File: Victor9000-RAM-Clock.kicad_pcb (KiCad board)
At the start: 2 copper layers, 1 part

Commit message: Layout
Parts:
- removed REF**: Victor 9000 Expansion Edge Connector, victor-exp:Victor Expansion Edge Connector
- added C1: 100n, Capacitor_THT:C_Disc_D5.0mm_W2.5mm_P2.50mm, F.Cu at (141.0, 83.8)
- added C2: 100n, Capacitor_THT:C_Disc_D5.0mm_W2.5mm_P2.50mm, F.Cu at (134.7, 132.1)
- added C3: 100n, Capacitor_THT:C_Disc_D5.0mm_W2.5mm_P2.50mm, F.Cu at (148.6, 132.1)
- added C4: 100n, Capacitor_THT:C_Disc_D5.0mm_W2.5mm_P2.50mm, F.Cu at (162.6, 132.1)
- added C5: 100n, Capacitor_THT:C_Disc_D5.0mm_W2.5mm_P2.50mm, F.Cu at (88.9, 132.1)
- added C6: 100n, Capacitor_THT:C_Disc_D5.0mm_W2.5mm_P2.50mm, F.Cu at (113.1, 132.1)
- added C7: 100n, Capacitor_THT:C_Disc_D5.0mm_W2.5mm_P2.50mm, F.Cu at (141.0, 96.5)
- added C8: 10u, Capacitor_THT:CP_Radial_D4.0mm_P1.50mm, F.Cu at (142.2, 132.1)
- added H1: Expansion_Connector, victor-exp:Victor Expansion Edge Connector, F.Cu at (108.0, 138.4)
- added JP1: Jumper, Connector_PinHeader_2.54mm:PinHeader_1x02_P2.54mm_Vertical, F.Cu at (127.0, 115.6)
- added R1: 10k, Resistor_THT:R_Axial_DIN0207_L6.3mm_D2.5mm_P7.62mm_Horizontal, F.Cu at (127.0, 132.1)
- added U1: 74LS00, Package_DIP:DIP-14_W7.62mm, F.Cu at (167.6, 127.0)
- added U2: 74LS11, Package_DIP:DIP-14_W7.62mm, F.Cu at (153.7, 127.0)
- added U3: 74LS139, Package_DIP:DIP-16_W7.62mm, F.Cu at (139.7, 127.0)
- added U4: 74LS373, Package_DIP:DIP-20_W7.62mm, F.Cu at (144.8, 104.1)
- added U5: AS6C4008-55PCN, Package_DIP:DIP-32_W15.24mm, F.Cu at (121.9, 127.0)
- added U6: 74LS245, Package_DIP:DIP-20_W7.62mm, F.Cu at (144.8, 91.4)
- added U7: AS6C4008-55PCN, Package_DIP:DIP-32_W15.24mm, F.Cu at (97.8, 127.0)
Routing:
- net /DT_~R: track 0.00 -> 115.4 mm, vias 0 -> 2
- net /ALE: track 0.00 -> 100.9 mm, vias 0 -> 2
- net /DQ7: track 0.00 -> 98.4 mm
- net /DQ6: track 0.00 -> 90.8 mm
- net /~EN2: track 0.00 -> 88.2 mm, vias 0 -> 1
- net /A19: track 0.00 -> 86.7 mm, vias 0 -> 1
- net /A17: track 0.00 -> 83.7 mm, vias 0 -> 1
- net /DQ5: track 0.00 -> 83.2 mm
- net /DQ0: track 0.00 -> 78.8 mm
- net /A7: track 0.00 -> 78.8 mm, vias 0 -> 1
- net /~EN1: track 0.00 -> 77.7 mm, vias 0 -> 1
- net /A3: track 0.00 -> 76.3 mm
- net /DQ4: track 0.00 -> 75.5 mm
- net /A18: track 0.00 -> 71.5 mm
- net /DQ1: track 0.00 -> 71.2 mm
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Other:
- net class Default: clearance 0.2 -> 0.254; trace_width 0.25 -> 0.254; via_dia 0.8 -> 0.762; via_drill 0.4 -> 0.381
- rule trace_clearance: 0.2 -> 0.254

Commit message: Routing completed
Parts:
- moved C3 26.5 mm to (159.4, 107.9), turned to 90 degrees
- moved C4 25.2 mm to (179.1, 113.0)
- moved C6 25.2 mm to (129.6, 113.0)
- moved C5 25.2 mm to (105.5, 113.0)
- moved U1 25.2 mm to (184.2, 108.0)
- moved U2 25.2 mm to (170.2, 108.0)
- moved U3 25.2 mm to (156.2, 108.0)
- moved C2 25.2 mm to (151.2, 113.0)
- moved H1 25.2 mm to (124.5, 119.4)
- moved R1 25.2 mm to (143.5, 113.0)
- moved U5 25.2 mm to (138.4, 108.0)
- moved C1 25.2 mm to (157.5, 64.8)
- moved C7 25.2 mm to (157.5, 77.5)
- moved JP1 25.2 mm to (143.5, 96.5)
- moved U4 25.2 mm to (161.3, 85.1)
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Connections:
- H1 pad 31: Net-(H1-Pad31) -> GND
- H1 pad 35: Net-(H1-Pad35) -> GND
- H1 pad 36: Net-(H1-Pad36) -> +5V
- H1 pad 39: Net-(H1-Pad39) -> GND
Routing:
- net +5V: track 0.00 -> 76.3 mm, vias 0 -> 2
- net GND: track 0.00 -> 41.2 mm, vias 0 -> 1
- added copper zone on F.Cu, net +5V
- added copper zone on B.Cu, net GND
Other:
- board outline added: 94 x 68.6 mm
- board text added: "Victor 9000 RAM Expansion v01 (c) Florian Reitz 2021"
- board text added: "v01"

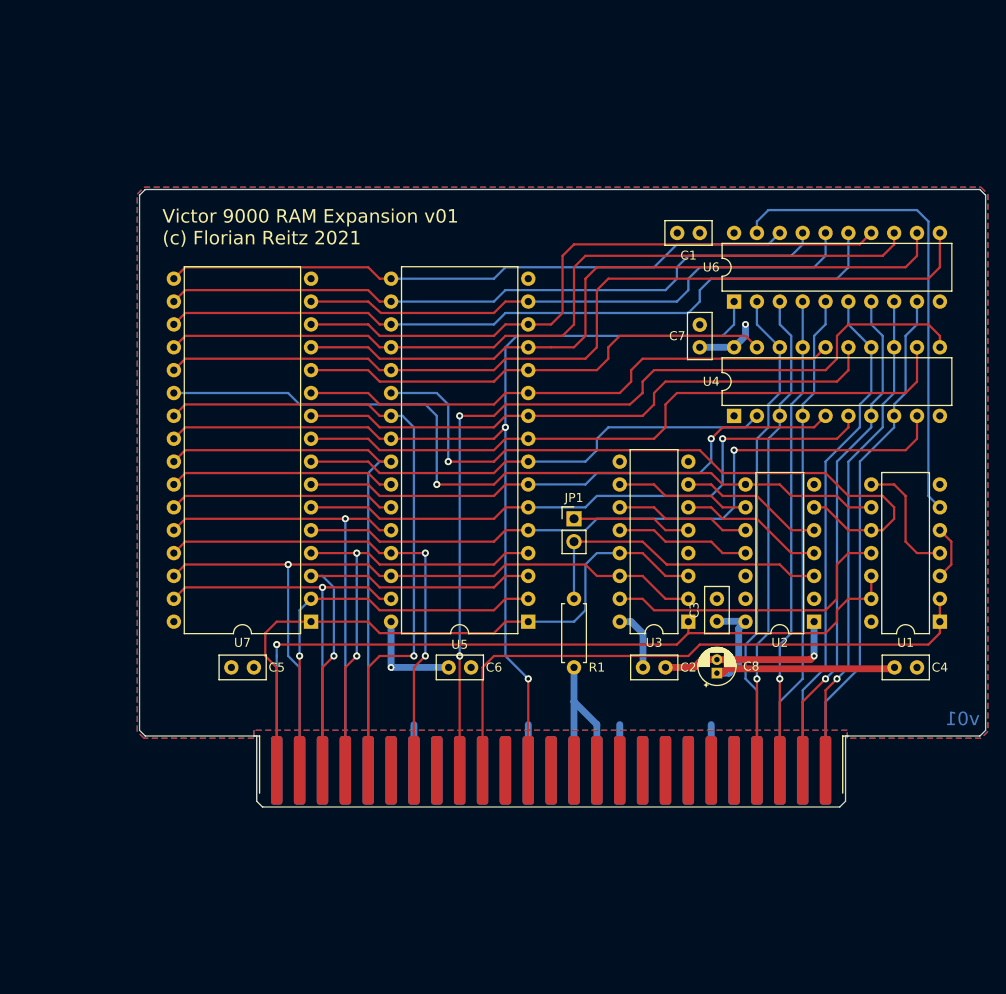
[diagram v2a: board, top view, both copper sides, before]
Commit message: DS1315 added
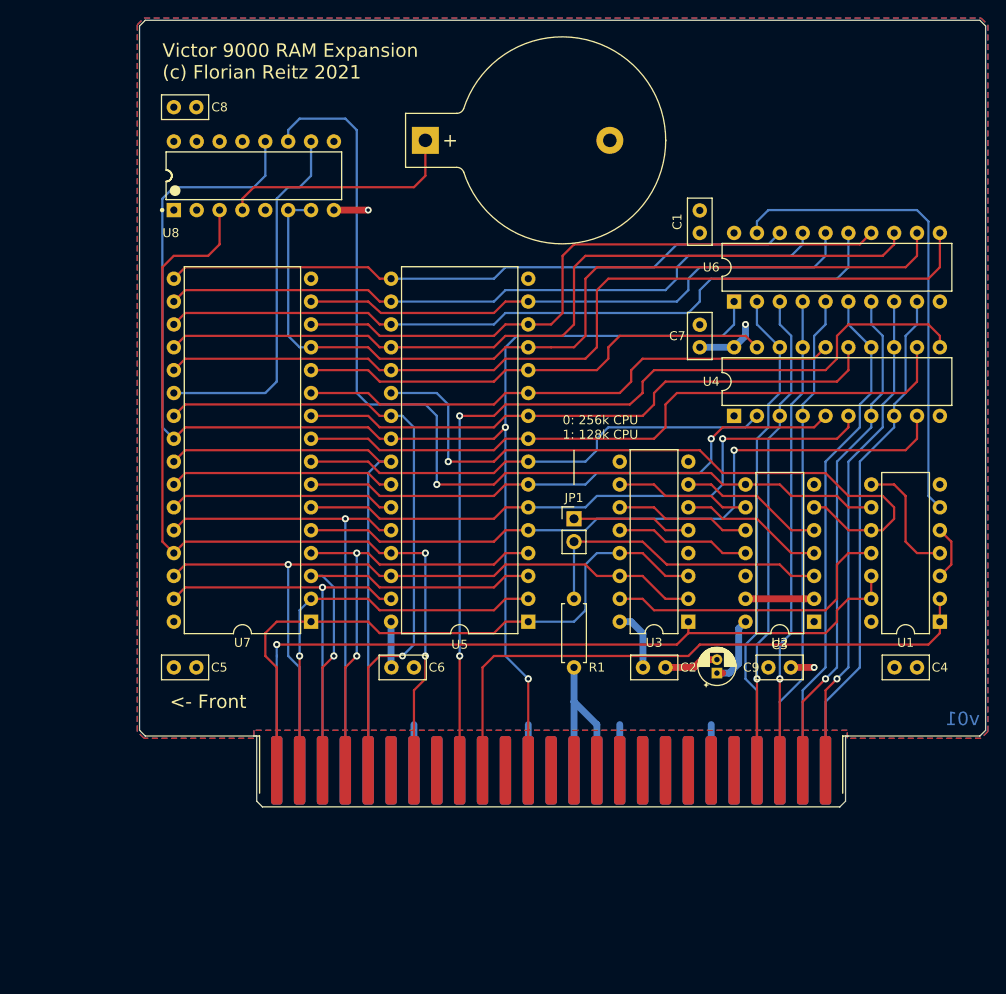
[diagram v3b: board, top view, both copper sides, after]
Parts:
- added BT1: Battery_Cell, Battery:BatteryHolder_Keystone_103_1x20mm, F.Cu at (127.0, 54.5)
- added C8: 100n, Capacitor_THT:C_Disc_D5.0mm_W2.5mm_P2.50mm, F.Cu at (99.1, 50.8)
- added U8: DS1315-5+, eec:Maxim-DS1315-5+-Manufacturer_Recommended, F.Cu at (99.1, 62.2)
- moved C3 7.67 mm to (165.1, 113.0), turned to 0 degrees
- moved R1 7.62 mm to (143.5, 105.4), turned to 270 degrees
- moved C5 6.39 mm to (99.1, 113.0)
- moved C6 6.35 mm to (123.2, 113.0)
- turned C1 to 90 degrees
- renumbered C8 to C9
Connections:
- net Net-(H1-Pad13) renamed /RESET
- R1 pad 1: +5V -> Net-(JP1-Pad2)
- R1 pad 2: Net-(JP1-Pad2) -> +5V
- U7 pad 22: /~EN2 -> /~EN2_B
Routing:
- net /DT_~R: track 115.4 -> 158.9 mm
- net /~SSO: track 53.6 -> 97.1 mm
- net /~EN2_B: track 0.00 -> 40.9 mm
- net +5V: track 76.3 -> 47.7 mm, vias 2 -> 1
- net Net-(BT1-Pad1): track 0.00 -> 26.6 mm
- net /DQ0: track 78.8 -> 98.4 mm
- net /~EN2: track 88.2 -> 107.1 mm
- net GND: track 41.2 -> 40.4 mm, vias 1 -> 2
- net /A10: track 70.7 -> 69.9 mm
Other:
- board size 94 x 68.6 mm -> 94 x 87.4 mm
- board text added: "0: 256k CPU 1: 128k CPU"
- board text added: "<- Front"
- board text added: "Victor 9000 RAM Expansion (c) Florian Reitz 2021"
- board text removed: "Victor 9000 RAM Expansion v01 (c) Florian Reitz 2021"

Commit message: Comments added
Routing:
- net /~SSO: track 97.1 -> 99.7 mm
- net /DT_~R: track 158.9 -> 161.5 mm
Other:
- board size 94 x 87.4 mm -> 95.2 x 87.4 mm
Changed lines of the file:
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@@
     (thickness 1.6)
     (drawings 19)
-    (tracks 605)
+    (tracks 607)
     (zones 0)
     (modules 21)
@@
   )
   (setup
-    (last_trace_width 0.762)
+    (last_trace_width 0.254)
     (user_trace_width 0.762)
     (trace_clearance 0.254)
@@
   (gr_line (start 188.595 120.65) (end 189.23 120.015) (layer Edge.Cuts) (width 0.0254))
   (gr_line (start 188.595 41.148) (end 189.23 41.783) (layer Edge.Cuts) (width 0.0254))
-  (gr_line (start 95.885 41.148) (end 95.25 41.783) (layer Edge.Cuts) (width 0.0254))
-  (gr_line (start 95.885 120.65) (end 95.25 120.015) (layer Edge.Cuts) (width 0.0254))
+  (gr_line (start 94.615 41.148) (end 93.98 41.783) (layer Edge.Cuts) (width 0.0254))
+  (gr_line (start 94.615 120.65) (end 93.98 120.015) (layer Edge.Cuts) (width 0.0254))
   (gr_line (start 108.9025 128.524) (end 108.2675 127.889) (layer Edge.Cuts) (width 0.0254))
   (gr_line (start 173.0375 128.524) (end 173.6725 127.889) (layer Edge.Cuts) (width 0.0254))
   (gr_line (start 189.23 120.015) (end 189.23 41.783) (layer Edge.Cuts) (width 0.0254))
   (gr_line (start 173.6725 120.65) (end 188.595 120.65) (layer Edge.Cuts) (width 0.0254))
-  (gr_line (start 95.885 41.148) (end 188.595 41.148) (layer Edge.Cuts) (width 0.0254))
-  (gr_line (start 95.25 120.015) (end 95.25 41.783) (layer Edge.Cuts) (width 0.0254))
-  (gr_line (start 108.2675 120.65) (end 95.885 120.65) (layer Edge.Cuts) (width 0.0254))
+  (gr_line (start 94.615 41.148) (end 188.595 41.148) (layer Edge.Cuts) (width 0.0254))
+  (gr_line (start 93.98 120.015) (end 93.98 41.783) (layer Edge.Cuts) (width 0.0254))
+  (gr_line (start 108.2675 120.65) (end 94.615 120.65) (layer Edge.Cuts) (width 0.0254))
   (gr_line (start 108.2675 127.889) (end 108.2675 120.65) (layer Edge.Cuts) (width 0.0254))
   (gr_line (start 173.6725 127.889) (end 173.6725 120.65) (layer Edge.Cuts) (width 0.0254))
@@
   (via (at 135.89 86.36) (size 0.8) (drill 0.4) (layers F.Cu B.Cu) (net 34))
   (segment (start 135.89 111.76) (end 135.89 86.36) (width 0.25) (layer B.Cu) (net 34))
+  (segment (start 107.95 59.69) (end 109.22 58.42) (width 0.254) (layer B.Cu) (net 34))
+  (segment (start 97.79 59.69) (end 107.95 59.69) (width 0.254) (layer B.Cu) (net 34))
   (segment (start 109.22 58.42) (end 109.22 54.61) (width 0.254) (layer B.Cu) (net 34))
-  (segment (start 107.95 59.69) (end 109.22 58.42) (width 0.254) (layer B.Cu) (net 34))
-  (segment (start 99.06 59.69) (end 107.95 59.69) (width 0.254) (layer B.Cu) (net 34))
-  (segment (start 97.79 60.96) (end 99.06 59.69) (width 0.254) (layer B.Cu) (net 34))
-  (segment (start 97.79 86.36) (end 97.79 60.96) (width 0.254) (layer B.Cu) (net 34))
-  (segment (start 99.06 87.63) (end 97.79 86.36) (width 0.254) (layer B.Cu) (net 34))
+  (segment (start 99.06 87.63) (end 97.79 87.63) (width 0.254) (layer B.Cu) (net 34))
+  (segment (start 96.52 60.96) (end 97.79 59.69) (width 0.254) (layer B.Cu) (net 34))
+  (segment (start 96.52 86.36) (end 96.52 60.96) (width 0.254) (layer B.Cu) (net 34))
+  (segment (start 97.79 87.63) (end 96.52 86.36) (width 0.254) (layer B.Cu) (net 34))
   (segment (start 184.15 107.95) (end 184.15 105.41) (width 0.25) (layer F.Cu) (net 36))
   (segment (start 184.15 109.22) (end 184.15 107.95) (width 0.25) (layer F.Cu) (net 36))
@@
   (via (at 127 111.76) (size 0.8) (drill 0.4) (layers F.Cu B.Cu) (net 39))
   (segment (start 127 100.33) (end 127 111.76) (width 0.25) (layer B.Cu) (net 39))
-  (segment (start 104.14 66.04) (end 104.14 62.23) (width 0.254) (layer F.Cu) (net 39))
-  (segment (start 97.79 68.58) (end 99.06 67.31) (width 0.254) (layer F.Cu) (net 39))
-  (segment (start 97.79 99.06) (end 97.79 68.58) (width 0.254) (layer F.Cu) (net 39))
-  (segment (start 102.87 67.31) (end 104.14 66.04) (width 0.254) (layer F.Cu) (net 39))
-  (segment (start 99.06 67.31) (end 102.87 67.31) (width 0.254) (layer F.Cu) (net 39))
-  (segment (start 99.06 100.33) (end 97.79 99.06) (width 0.254) (layer F.Cu) (net 39))
   (segment (start 127 111.76) (end 127 114.3) (width 0.254) (layer F.Cu) (net 39))
   (segment (start 127 114.3) (end 125.73 115.57) (width 0.254) (layer F.Cu) (net 39))
   (segment (start 125.73 115.57) (end 125.73 124.46) (width 0.254) (layer F.Cu) (net 39))
+  (segment (start 104.14 66.04) (end 104.14 62.23) (width 0.254) (layer F.Cu) (net 39))
+  (segment (start 97.79 67.31) (end 102.87 67.31) (width 0.254) (layer F.Cu) (net 39))
+  (segment (start 102.87 67.31) (end 104.14 66.04) (width 0.254) (layer F.Cu) (net 39))
+  (segment (start 96.52 99.06) (end 96.52 68.58) (width 0.254) (layer F.Cu) (net 39))
+  (segment (start 96.52 68.58) (end 97.79 67.31) (width 0.254) (layer F.Cu) (net 39))
+  (segment (start 96.52 99.06) (end 97.79 100.33) (width 0.254) (layer F.Cu) (net 39))
+  (segment (start 97.79 100.33) (end 99.06 100.33) (width 0.254) (layer F.Cu) (net 39))
   (segment (start 99.06 85.09) (end 100.33 83.82) (width 0.25) (layer F.Cu) (net 41))
   (segment (start 100.33 83.82) (end 120.65 83.82) (width 0.25) (layer F.Cu) (net 41))
@@
       (pts
         (xy 189.484 41.656) (xy 189.484 120.142) (xy 188.722 120.904) (xy 173.863 120.904) (xy 173.863 120.015)
-        (xy 107.95 120.015) (xy 107.95 120.904) (xy 95.758 120.904) (xy 94.996 120.142) (xy 94.996 41.656)
-        (xy 95.758 40.894) (xy 188.722 40.894)
+        (xy 107.95 120.015) (xy 107.95 120.904) (xy 94.488 120.904) (xy 93.726 120.142) (xy 93.726 41.656)
+        (xy 94.488 40.894) (xy 188.722 40.894)
       )
     )
@@
       (pts
         (xy 189.484 41.656) (xy 189.484 120.142) (xy 188.722 120.904) (xy 173.863 120.904) (xy 173.863 120.015)
-        (xy 107.95 120.015) (xy 107.95 120.904) (xy 95.758 120.904) (xy 94.996 120.142) (xy 94.996 41.656)
-        (xy 95.758 40.894) (xy 188.722 40.894)
+        (xy 107.95 120.015) (xy 107.95 120.904) (xy 94.488 120.904) (xy 93.726 120.142) (xy 93.726 41.656)
+        (xy 94.488 40.894) (xy 188.722 40.894)
       )
     )

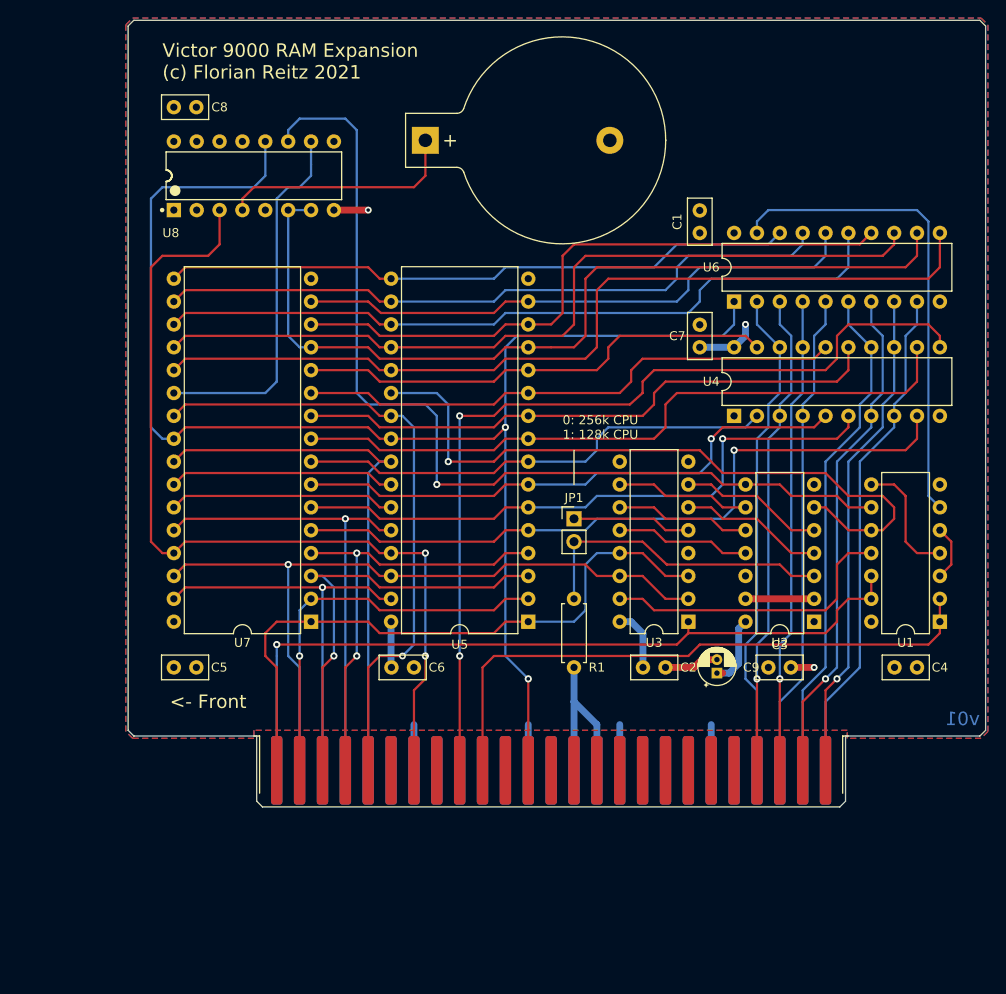
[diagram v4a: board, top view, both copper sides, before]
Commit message: Swapped layers
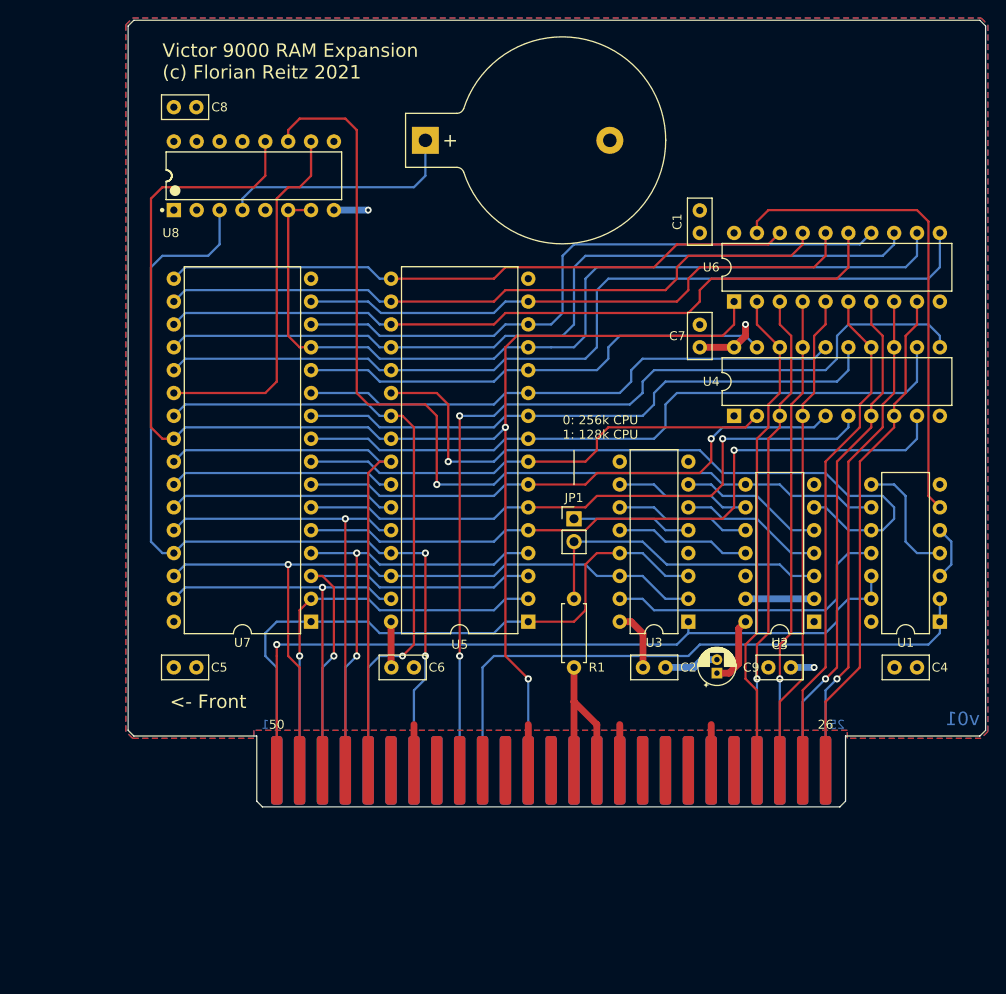
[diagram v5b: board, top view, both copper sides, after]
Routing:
- added copper zone on B.Cu, net +5V
- added copper zone on F.Cu, net GND
- removed copper zone on F.Cu, net +5V
- removed copper zone on B.Cu, net GND
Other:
- board text added: "1"
- board text added: "25"
- board text added: "26"
- board text added: "50"
